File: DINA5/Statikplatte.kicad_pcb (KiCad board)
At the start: 2 copper layers, 210 x 148 mm, 37 parts, among them J1 VIN, J10 HV, J11 SCREW, J12 SCREW, J13 SCREW, J14 SCREW, J2 GND, J3 GND, J4 GND, J5 GND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

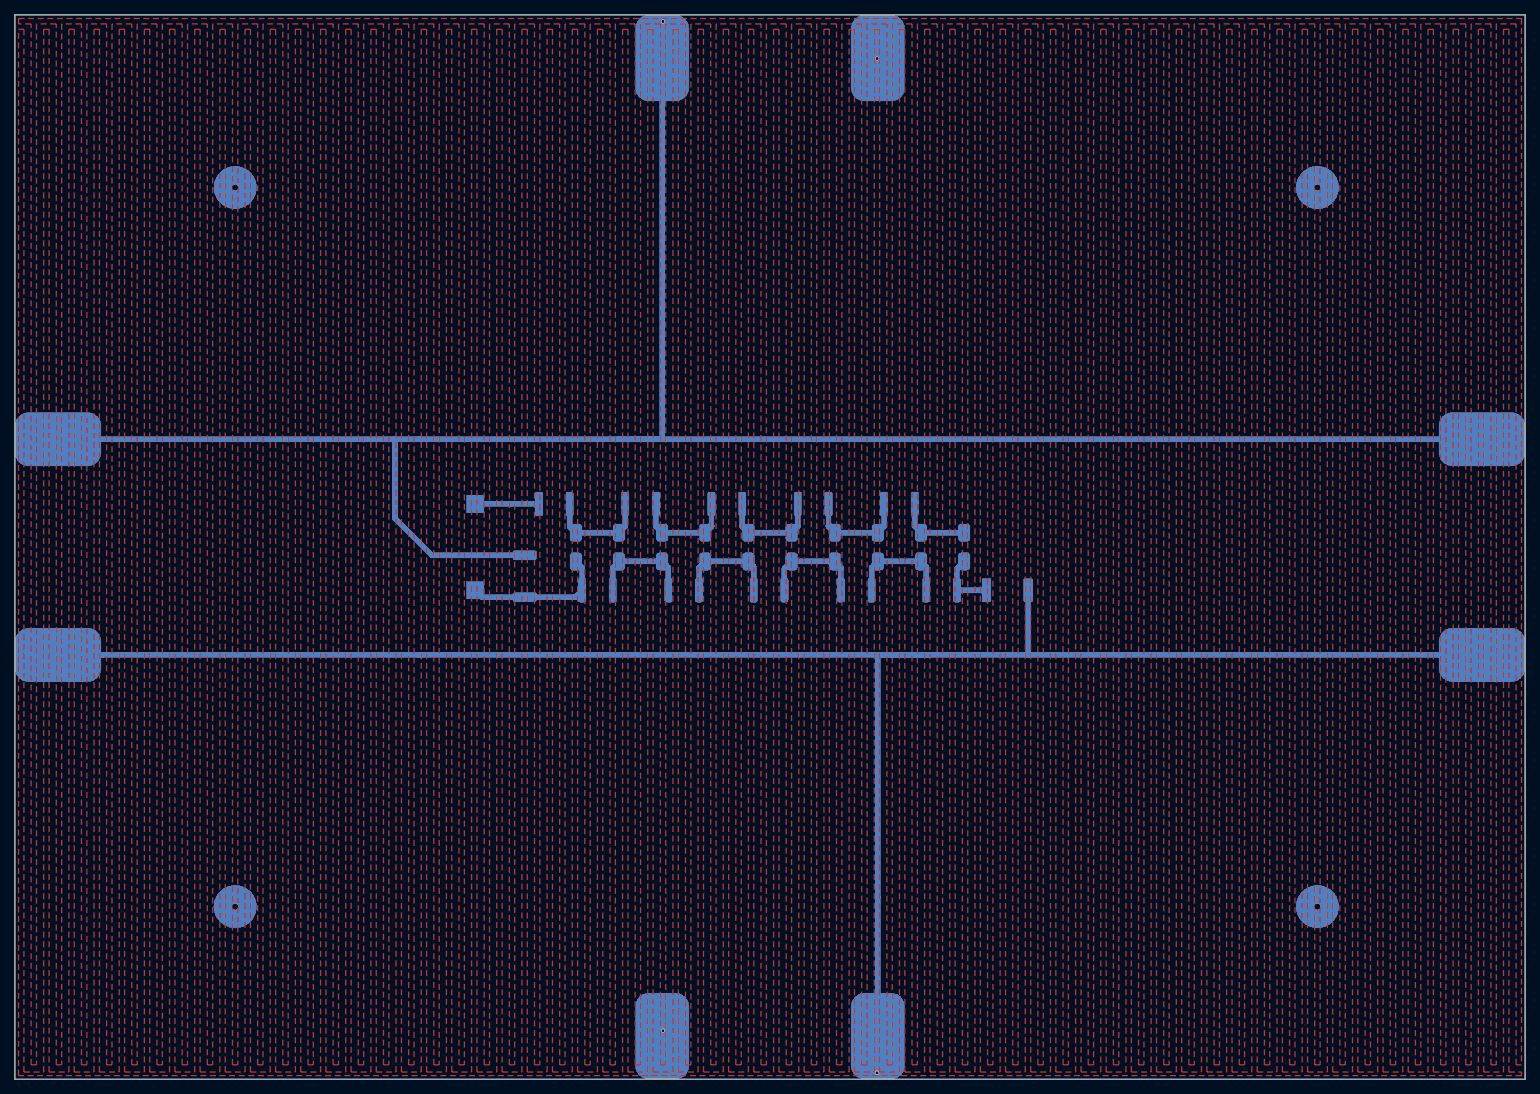
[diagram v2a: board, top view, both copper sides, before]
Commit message: added negative kaskade
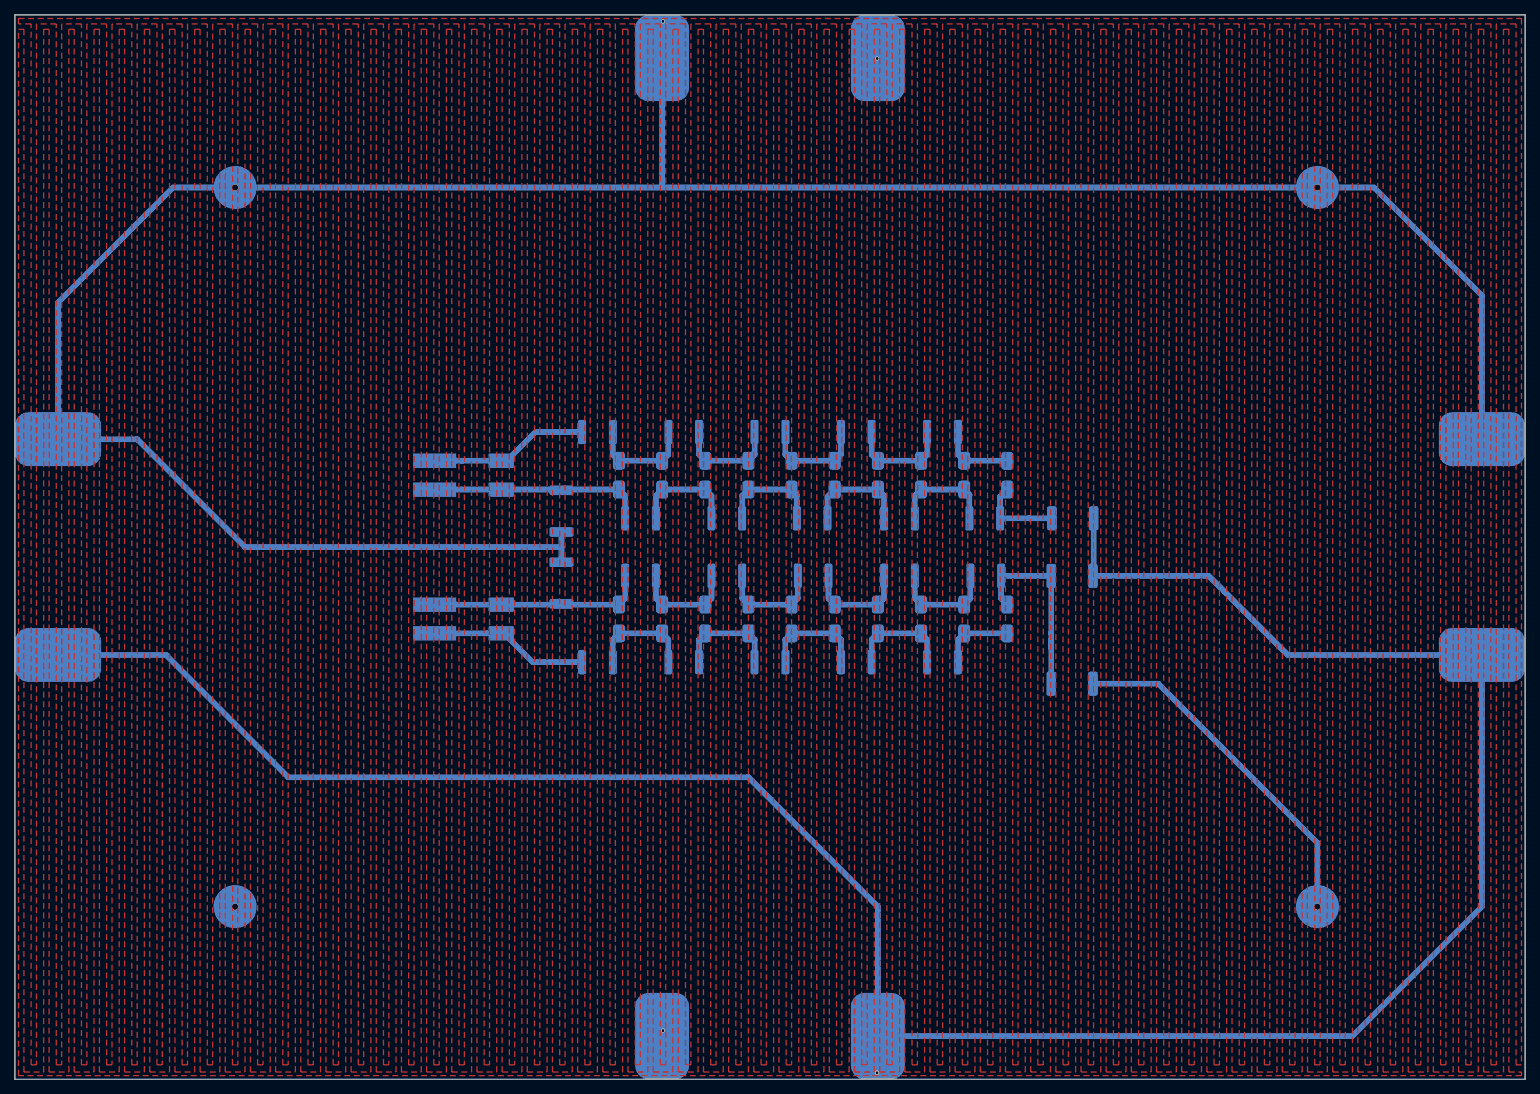
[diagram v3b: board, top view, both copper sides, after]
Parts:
- removed G***: LOGO, otter:otterimage
- added C11: 1n, Capacitor_SMD:C_1812_4532Metric, B.Cu at (96.0, 105.0)
- added C12: 1n, Capacitor_SMD:C_1812_4532Metric, B.Cu at (102.0, 93.0)
- added C13: 1n, Capacitor_SMD:C_1812_4532Metric, B.Cu at (108.0, 105.0)
- added C14: 1n, Capacitor_SMD:C_1812_4532Metric, B.Cu at (114.0, 93.0)
- added C15: 1n, Capacitor_SMD:C_1812_4532Metric, B.Cu at (120.0, 105.0)
- added C16: 1n, Capacitor_SMD:C_1812_4532Metric, B.Cu at (126.0, 93.0)
- added C17: 1n, Capacitor_SMD:C_1812_4532Metric, B.Cu at (132.0, 105.0)
- added C18: 1n, Capacitor_SMD:C_1812_4532Metric, B.Cu at (138.0, 93.0)
- added C19: 1n, Capacitor_SMD:C_1812_4532Metric, B.Cu at (144.0, 105.0)
- added C20: 1n, Capacitor_SMD:C_1812_4532Metric, B.Cu at (150.0, 93.0)
- added D11: D, otter:SMAF, B.Cu at (99.0, 99.0)
- added D12: D, otter:SMAF, B.Cu at (105.0, 99.0)
- added D13: D, otter:SMAF, B.Cu at (111.0, 99.0)
- added D14: D, otter:SMAF, B.Cu at (117.0, 99.0)
- added D15: D, otter:SMAF, B.Cu at (123.0, 99.0)
- added D16: D, otter:SMAF, B.Cu at (129.0, 99.0)
- added D17: D, otter:SMAF, B.Cu at (135.0, 99.0)
- added D18: D, otter:SMAF, B.Cu at (141.0, 99.0)
- added D19: D, otter:SMAF, B.Cu at (147.0, 99.0)
- added D20: D, otter:SMAF, B.Cu at (153.0, 99.0)
- added R3: 33M, Resistor_SMD:R_2512_6332Metric, B.Cu at (162.0, 93.0)
- added R4: 33M, Resistor_SMD:R_2512_6332Metric, B.Cu at (162.0, 108.0)
- added R5: 33M, Resistor_SMD:R_2512_6332Metric, B.Cu at (91.0, 94.0)
- J1: value VIN -> IN-; footprint TestPoint:TestPoint_Pad_2.5x2.5mm -> otter:LED_Connector
- J3: value GND -> IN+; footprint TestPoint:TestPoint_Pad_2.5x2.5mm -> otter:LED_Connector
- moved J1 16.0 mm to (78.0, 99.0), turned to 0 degrees
- moved J3 16.0 mm to (78.0, 79.0), turned to 0 degrees
- moved R1 13.5 mm to (162.1, 85.0)
- moved C1 11.7 mm to (96.0, 73.0)
- moved C10 11.7 mm to (149.9, 85.0)
- moved C2 11.7 mm to (102.0, 85.0)
- moved C3 11.7 mm to (108.0, 73.0)
- moved C4 11.7 mm to (114.0, 85.0)
- moved C5 11.7 mm to (120.0, 73.0)
- moved C6 11.7 mm to (125.9, 85.0)
- moved C7 11.7 mm to (132.0, 73.0)
- moved C8 11.7 mm to (138.0, 85.0)
- moved C9 11.7 mm to (144.0, 73.0)
- moved D1 11.7 mm to (99.0, 79.0)
- moved D10 11.7 mm to (153.0, 79.0)
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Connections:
- C1 pad 2: Net-(C1-Pad2) -> /IN1
- J1 pad 1: Net-(C1-Pad2) -> /IN2
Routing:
- net /GNDE: track 288.2 -> 398.5 mm
- net /HV: track 267.2 -> 341.1 mm
- net /GND1: track 0.00 -> 32.0 mm
- net /N10-: track 0.00 -> 27.3 mm
- net /IN1: track 0.00 -> 27.0 mm
- net /IN2: track 0.00 -> 24.1 mm
- net /N8-: track 0.00 -> 14.7 mm
- net /N2-: track 0.00 -> 14.7 mm
- net /N7-: track 0.00 -> 14.7 mm
- net /N6-: track 0.00 -> 14.7 mm
- net /N5-: track 0.00 -> 14.7 mm
- net /N4-: track 0.00 -> 14.7 mm
- net /N3-: track 0.00 -> 14.7 mm
- net /N1-: track 0.00 -> 14.7 mm
- net /N9-: track 0.00 -> 10.4 mm
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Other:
- board text added: "Negative Input"
- board text added: "Positive Input"

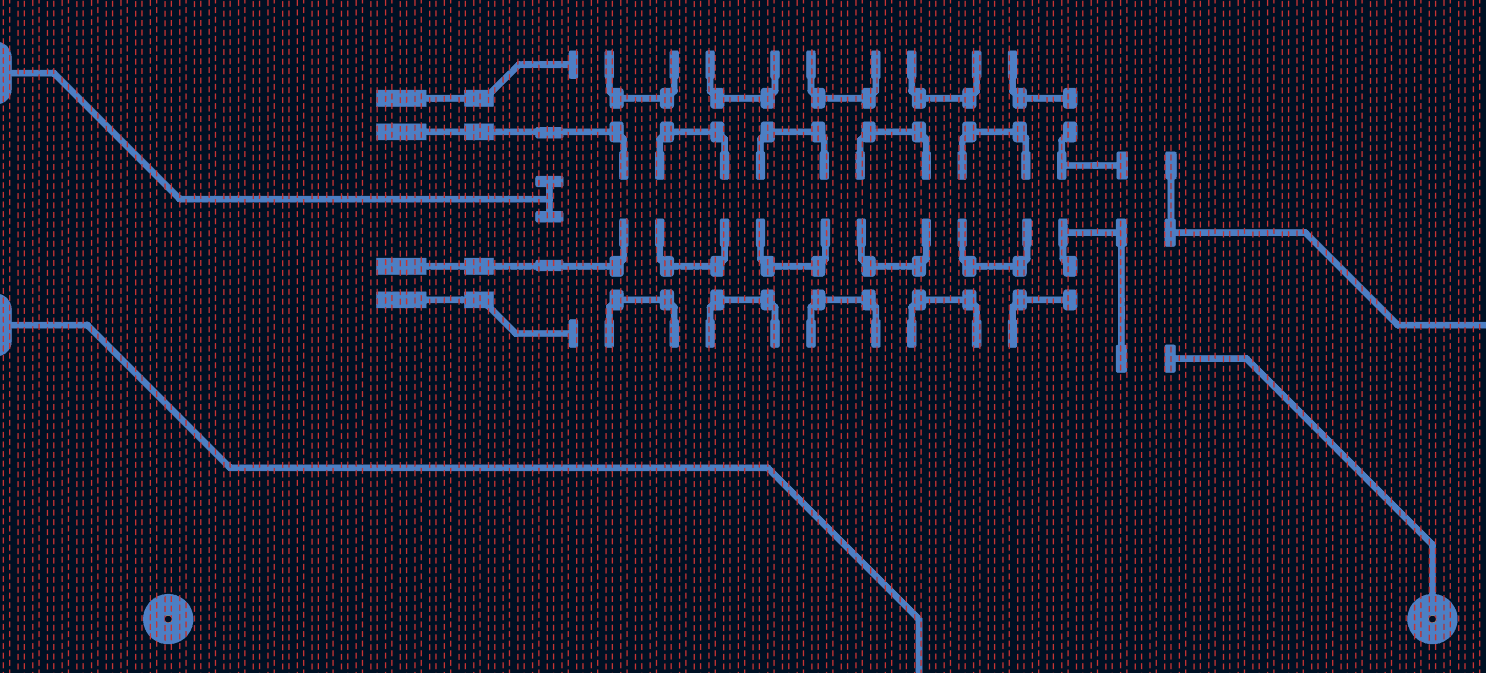
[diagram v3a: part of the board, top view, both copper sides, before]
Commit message: went back to one voltage multiplier
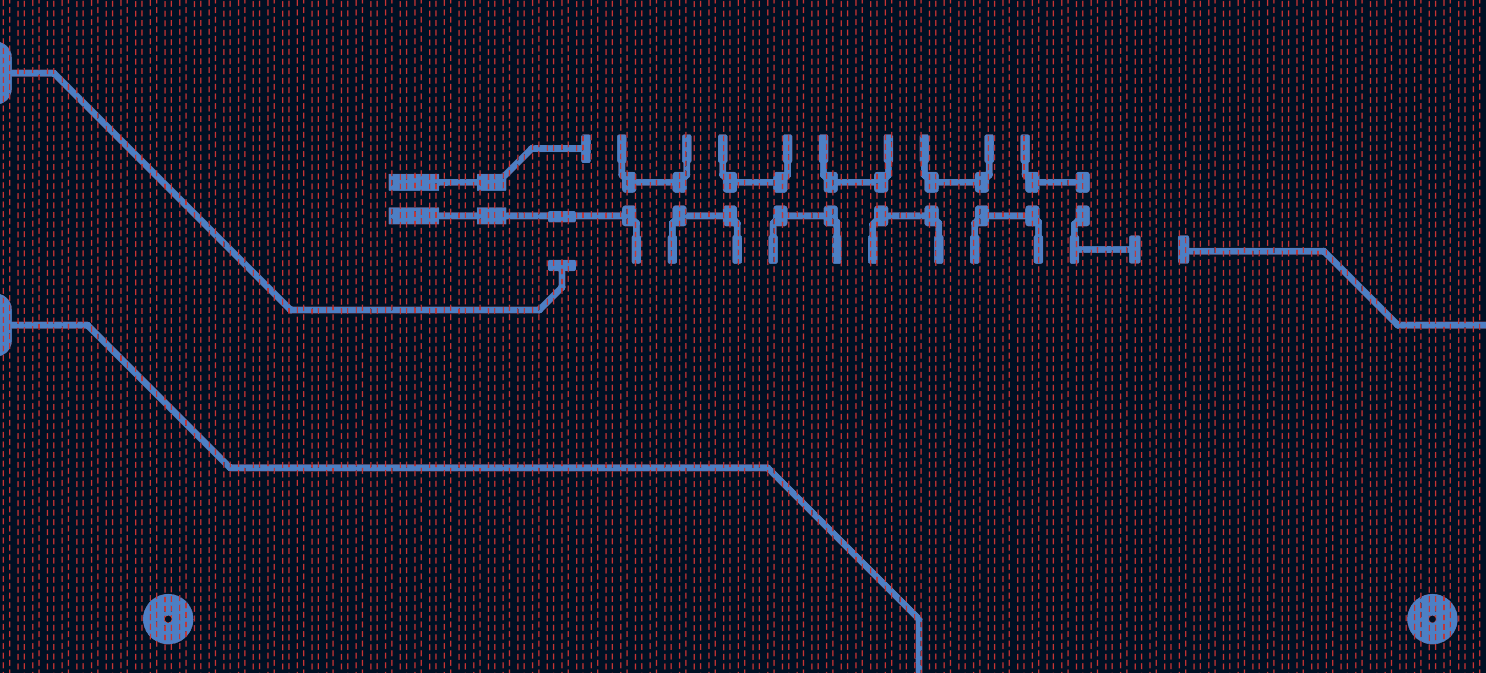
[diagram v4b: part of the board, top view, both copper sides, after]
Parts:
- removed C11, C12, C13, C14, C15, C16, C17, C18, C19, C20: 1n, Capacitor_SMD:C_1812_4532Metric
- removed D11, D12, D13, D14, D15, D16, D17, D18, D19, D20: D, otter:SMAF
- removed J1: IN-, otter:LED_Connector
- removed R3, R4, R5: 33M, Resistor_SMD:R_2512_6332Metric
- moved C1 10.1 mm to (97.5, 83.0)
- moved C10 10.1 mm to (151.4, 95.0)
- moved C2 10.1 mm to (103.5, 95.0)
- moved C3 10.1 mm to (109.5, 83.0)
- moved C4 10.1 mm to (115.5, 95.0)
- moved C5 10.1 mm to (121.5, 83.0)
- moved C6 10.1 mm to (127.4, 95.0)
- moved C7 10.1 mm to (133.5, 83.0)
- moved C8 10.1 mm to (139.5, 95.0)
- moved C9 10.1 mm to (145.5, 83.0)
- moved D1 10.1 mm to (100.5, 89.0)
- moved D10 10.1 mm to (154.5, 89.0)
- moved D2 10.1 mm to (106.5, 89.0)
- moved D3 10.1 mm to (112.5, 89.0)
- moved D4 10.1 mm to (118.5, 89.0)
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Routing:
- net /GNDE: track 398.5 -> 355.7 mm
- net /GND1: track 32.0 -> 0.00 mm
- net /N10-: track 27.3 -> 0.00 mm
- net /IN2: track 24.1 -> 0.00 mm
- net /N8-: track 14.7 -> 0.00 mm
- net /N2-: track 14.7 -> 0.00 mm
- net /N7-: track 14.7 -> 0.00 mm
- net /N6-: track 14.7 -> 0.00 mm
- net /N5-: track 14.7 -> 0.00 mm
- net /N4-: track 14.7 -> 0.00 mm
- net /N3-: track 14.7 -> 0.00 mm
- net /N1-: track 14.7 -> 0.00 mm
- net /HV: track 341.1 -> 330.6 mm
- net /N9-: track 10.4 -> 0.00 mm
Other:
- board text removed: "Negative Input"
- board text removed: "Positive Input"
